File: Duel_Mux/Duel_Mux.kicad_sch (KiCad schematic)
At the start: 7 parts, among them J1 Conn_01x08_Pin, J2 Conn_01x02_Pin, J3 2xRJ_45, J4 Conn_01x08_Pin, J5 Conn_01x03_Pin, U1 ADG406BNZ, U2 ADG406BNZ

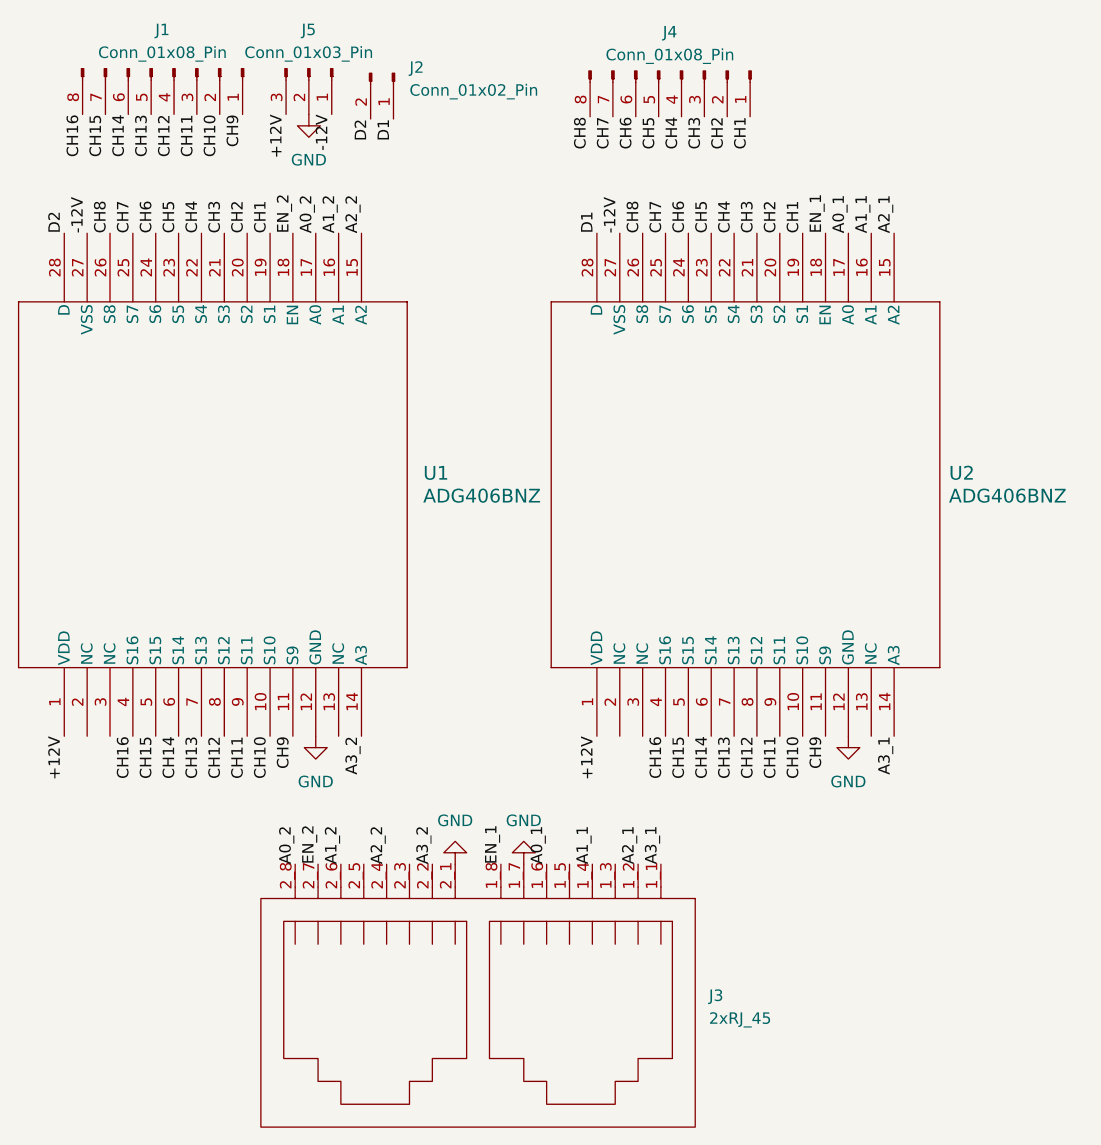
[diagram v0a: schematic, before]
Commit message: Push update demodulation error test and updated duel mux
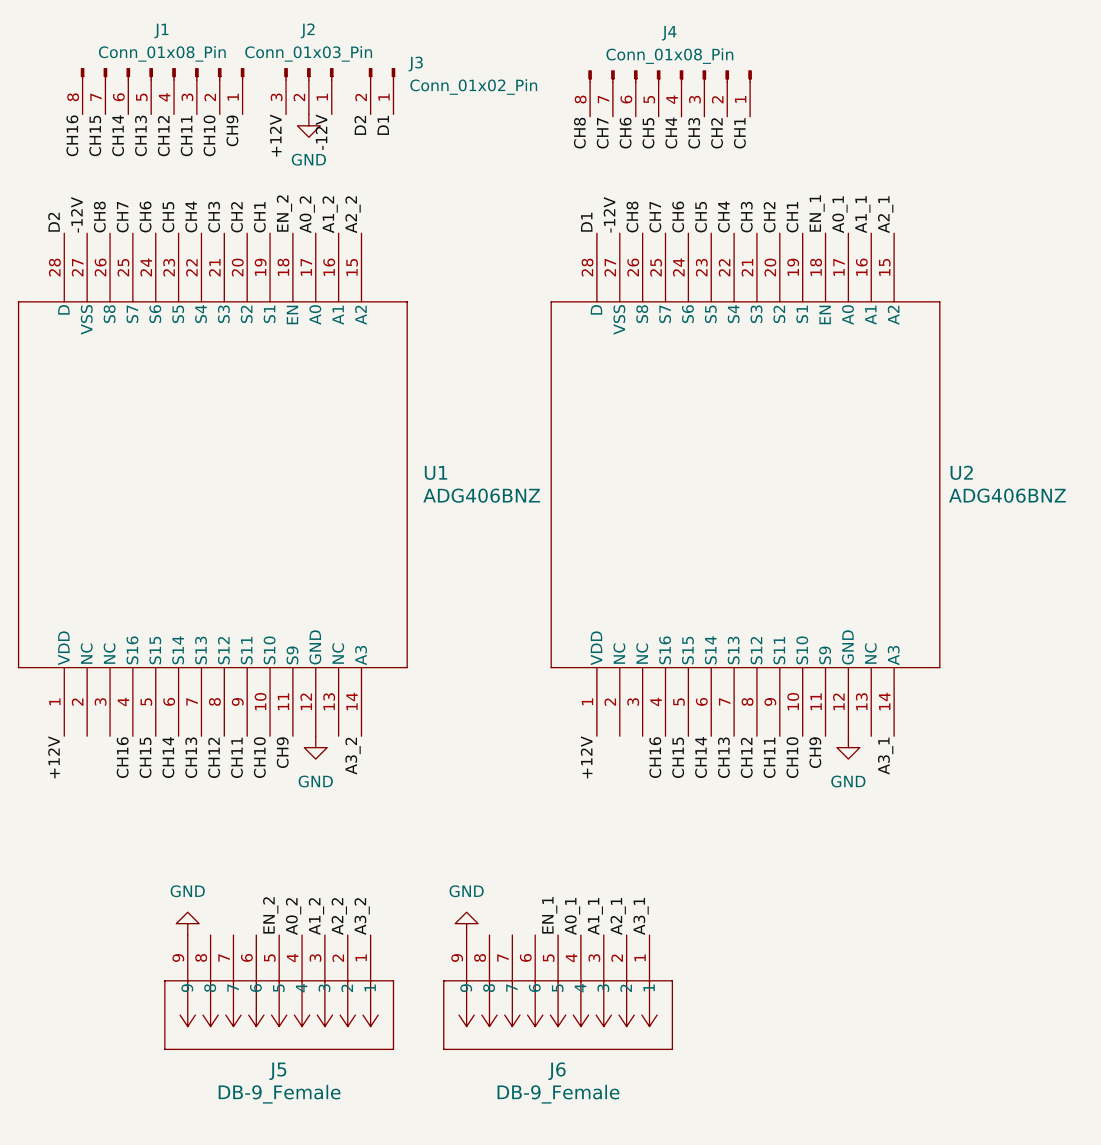
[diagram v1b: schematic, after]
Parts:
- removed J3: 2xRJ_45, TE_2xRJ45:TE_2xRJ45, symbol Duel_Ethernet_Port:Duel_Ethernet_Port
- added J5, J6: DB-9_Female, DB-9_Female:DB-9_Female, symbol DB-9_Female:DB-9_Female
- renumbered J5 to J2, J2 to J3
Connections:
- net A0_1: now also J6.4
- net A0_2: now also J5.4
- net A1_1: now also J6.3
- net A1_2: now also J5.3
- net A2_1: now also J6.2
- net A2_2: now also J5.2
- net A3_1: now also J6.1
- net A3_2: now also J5.1
- net EN_1: now also J6.5
- net EN_2: now also J5.5
- net GND: now also J5.9, J6.9
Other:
- moved on the sheet: J3
